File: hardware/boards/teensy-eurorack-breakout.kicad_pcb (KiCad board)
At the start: 4 copper layers, 110.5 x 111.1 mm, 75 parts, among them J1 Conn_01x08, SW1 Rotary_Encoder_Switch, SW2 Rotary_Encoder_Switch, SW3 Rotary_Encoder_Switch, U2 AD5754BREZ, U3 AD5754BREZ, U5 MCP1700-2502E, U6 AD7606BSTZ, U7 6N138

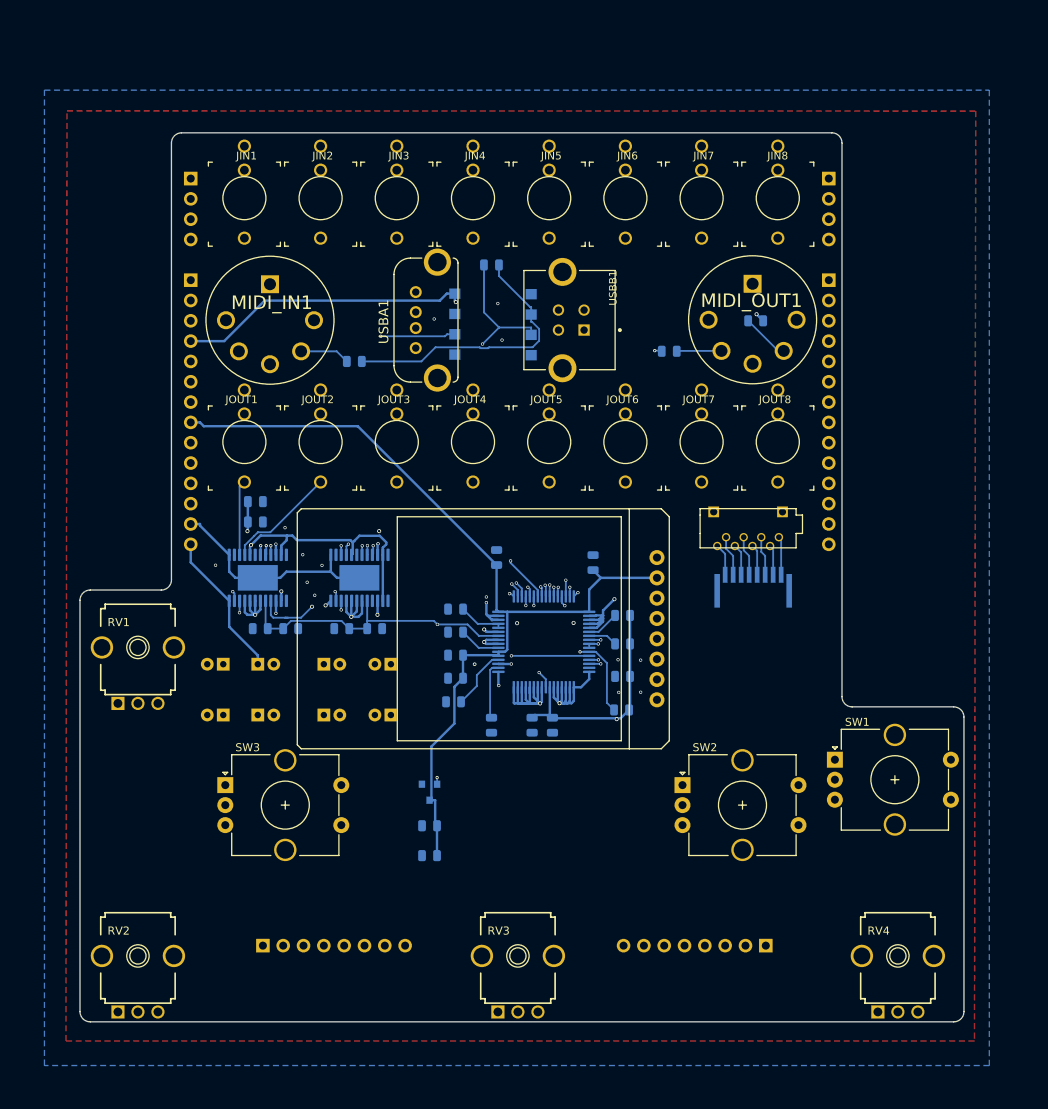
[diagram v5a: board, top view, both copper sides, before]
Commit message: pcb: update min via size to .45/.25 mm, routed as 4 layer
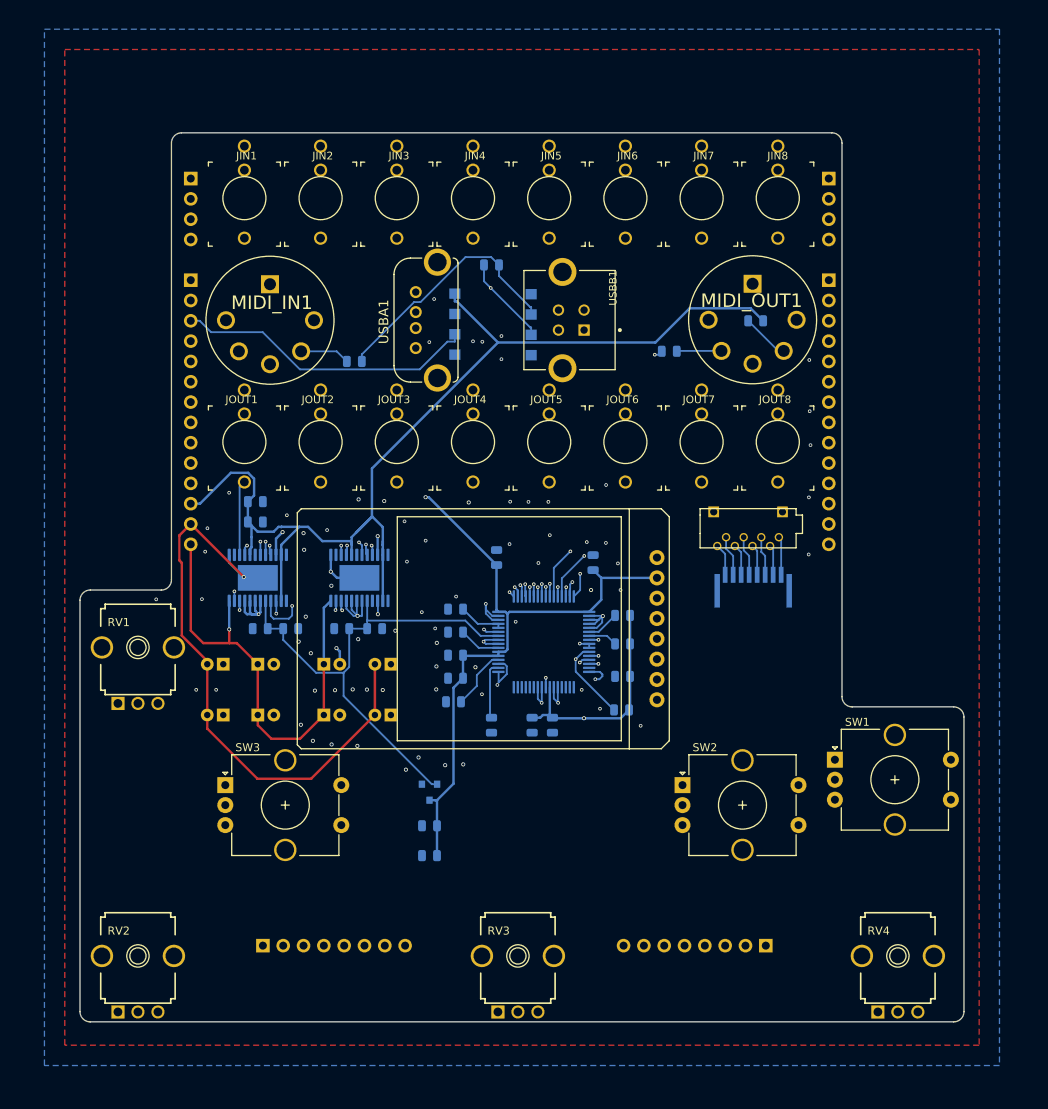
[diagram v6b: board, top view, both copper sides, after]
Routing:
- net GND: track 99.6 -> 65.4 mm, vias 31 -> 86
- net -12V: track 79.8 -> 106.5 mm, vias 0 -> 2
- net +12V: track 48.0 -> 58.6 mm
- net +3V3: track 383.0 -> 390.9 mm, vias 6 -> 1
- net /DAC_REF2V5: track 57.5 -> 64.1 mm, vias 2 -> 0
- net /DAC_SCK: track 64.0 -> 68.4 mm
- net /MIDI_RX: track 33.9 -> 37.9 mm, vias 1 -> 0
- net /VOUT3: track 31.0 -> 27.1 mm
- net Net-(D1-Pad1): track 35.0 -> 31.4 mm
- net /MIDI_TX: track 63.2 -> 65.7 mm, vias 2 -> 1
- net Net-(U2-Pad16): track 20.0 -> 22.3 mm
- net /VIN7: track 54.3 -> 52.0 mm
- net /VGND3: track 65.7 -> 63.4 mm
- net /VGND2: track 69.2 -> 66.9 mm
- net /ADC_CS: track 53.3 -> 54.6 mm
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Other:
- net class Default: via_dia 0.4 -> 0.45
- rule via_min_size: 0.4 -> 0.45

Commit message: soldermask clearance set to 0.05mm and minimum soldermask bridge to 0.2mm as per jlcpcb
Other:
- rule pad_to_mask_clearance: 0 -> 0.05

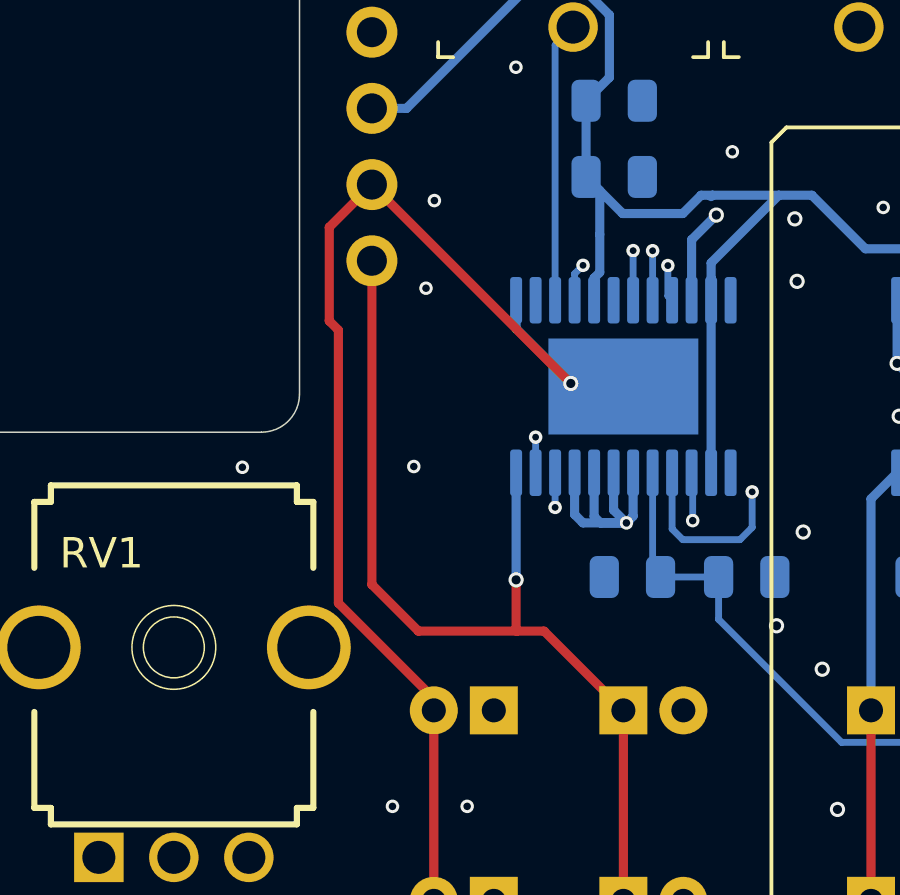
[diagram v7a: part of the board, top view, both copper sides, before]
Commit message: MAJOR: breakout PCB correction to polarity of +12V
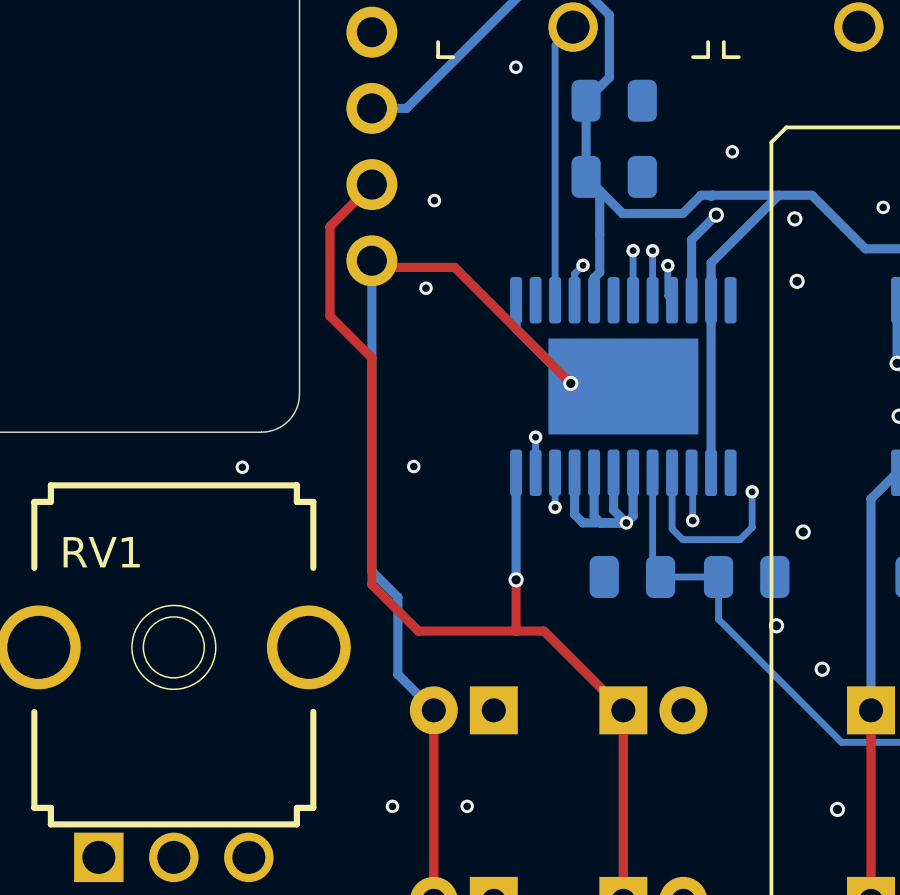
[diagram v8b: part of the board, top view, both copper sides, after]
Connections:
- JB1 pad 13: -12V -> +12V
- JB1 pad 14: +12V -> -12V
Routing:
- net -12V: track 106.5 -> 102.1 mm
- net +12V: track 58.6 -> 62.3 mm
